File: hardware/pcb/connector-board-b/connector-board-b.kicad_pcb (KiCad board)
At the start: 2 copper layers, 27.4 x 70.6 mm, 46 parts, among them J1 DE9_Pins, J2 PANEL_18V, J5 8-215570-0, J6 NTC_103AT, J7 BATTERY, Q1 Si4840BDY, Q2 Si4840BDY, SW1 PWR_KILL, U1 BQ24650RVA, U2 INA3221, U3 MCP1700-3.3

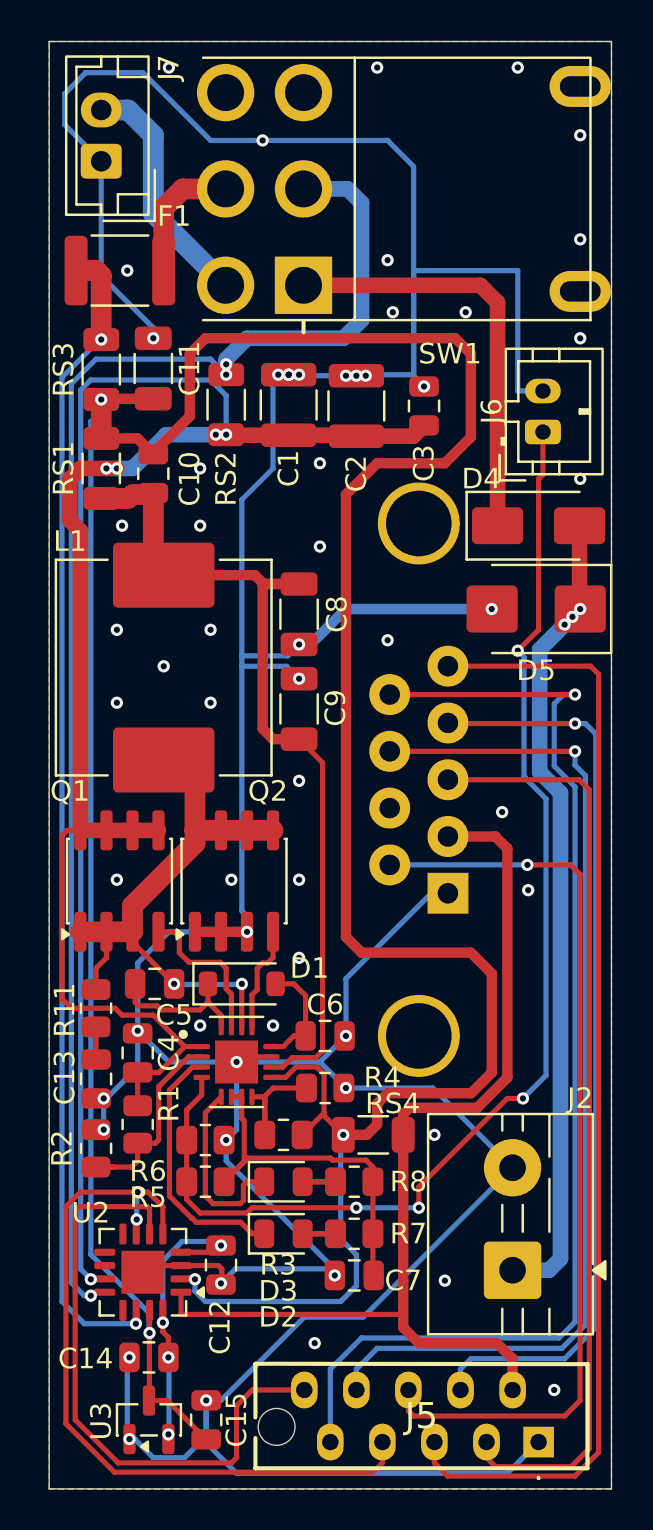
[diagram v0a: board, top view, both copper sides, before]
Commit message: Changed via placements to avoid solderwicking
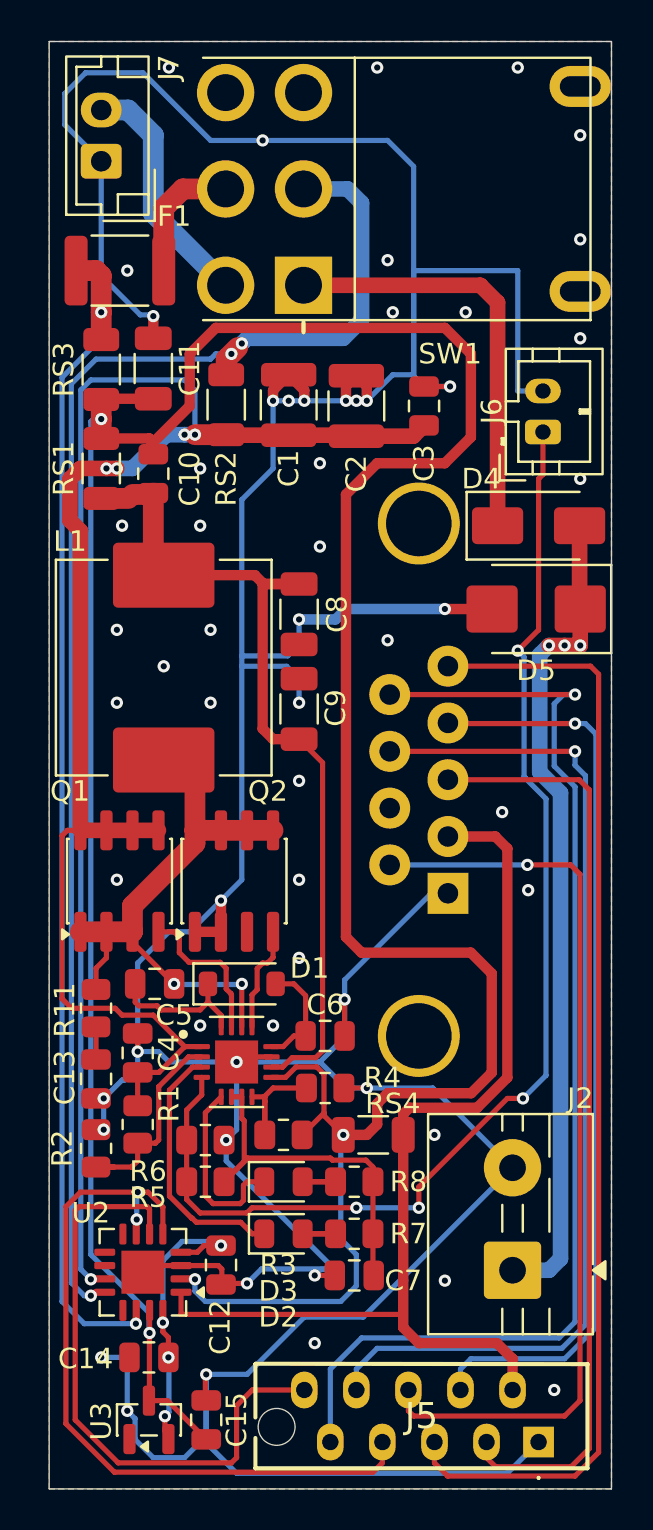
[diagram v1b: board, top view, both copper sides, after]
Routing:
- net GND: track 239.2 -> 256.5 mm, vias 61 -> 59
- net VIN: track 114.0 -> 112.7 mm
- net VBAT: track 56.9 -> 58.2 mm
- net Net-(D4-A): track 39.6 -> 40.5 mm
- net VCC: track 162.1 -> 161.5 mm

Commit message: Parts ordered!
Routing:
- net GND: track 256.5 -> 275.0 mm
- net VCC: track 161.5 -> 167.0 mm
- net PANEL+: track 71.7 -> 73.8 mm
- net Net-(U1-PH): track 29.5 -> 30.9 mm
- net Net-(D3-K): track 9.06 -> 10.2 mm
- net VIN: track 112.7 -> 113.5 mm
- net VLOAD+: track 51.6 -> 52.4 mm
- net VBAT: track 58.2 -> 58.7 mm
